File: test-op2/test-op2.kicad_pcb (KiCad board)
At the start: 2 copper layers, 167 parts, among them P1 In1, P10 Out2, P11 Out3, P12 Out4, P13 CONN_13X2, P14 CONN_5X2, P2 In2, P3 In3, P4 In4, P5 HOLD3, P6 RST3, P7 HOLD4, P8 RST4, P9 Out1, U1 LM7171, U10 LM7171, U11 LMH6505, U12 LMH6505, U13 DG467, U14 DG468, U15 LM7171, U16 LMH6505, U17 LMH6505, U2 LMH6505, U3 LMH6505, U4 LM7171, U5 LMH6505, U6 LMH6505, U7 DG467, U8 DG468, U9 LM7171

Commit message: [test-op2] layout
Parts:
- moved C64 0.13 mm to (148.2, 39.2), turned to 0 degrees
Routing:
- net GND: track 137.5 -> 957.2 mm, vias 0 -> 13
- net +5V: track 40.8 -> 382.2 mm, vias 0 -> 11
- net -5V: track 32.8 -> 258.6 mm, vias 0 -> 19
- net Off1_3: track 2.35 -> 192.0 mm, vias 0 -> 1
- net +15V: track 11.4 -> 193.0 mm, vias 0 -> 1
- net Ctrl1_1: track 0.00 -> 135.0 mm, vias 0 -> 1
- net Off1_4: track 2.17 -> 136.6 mm, vias 0 -> 1
- net -15V: track 13.4 -> 132.7 mm, vias 0 -> 7
- net Off2_1: track 3.53 -> 108.6 mm
- net Ctrl1_4: track 0.00 -> 97.7 mm, vias 0 -> 4
- net Off1_1: track 2.43 -> 98.7 mm
- net Off2_4: track 1.99 -> 96.6 mm, vias 0 -> 1
- net Off1_2: track 2.43 -> 93.4 mm, vias 0 -> 1
- net Off3_4: track 0.00 -> 89.8 mm, vias 0 -> 2
- net Off4_1: track 2.63 -> 86.9 mm, vias 0 -> 1
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- added copper zone on B.Cu, net GND
- added copper zone on F.Cu, net GND

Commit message: [test-op2] tweak
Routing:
- net Off1_3: track 192.0 -> 192.8 mm
- net Off1_4: track 136.6 -> 137.3 mm
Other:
- board outline added: 137.8 x 75.6 mm

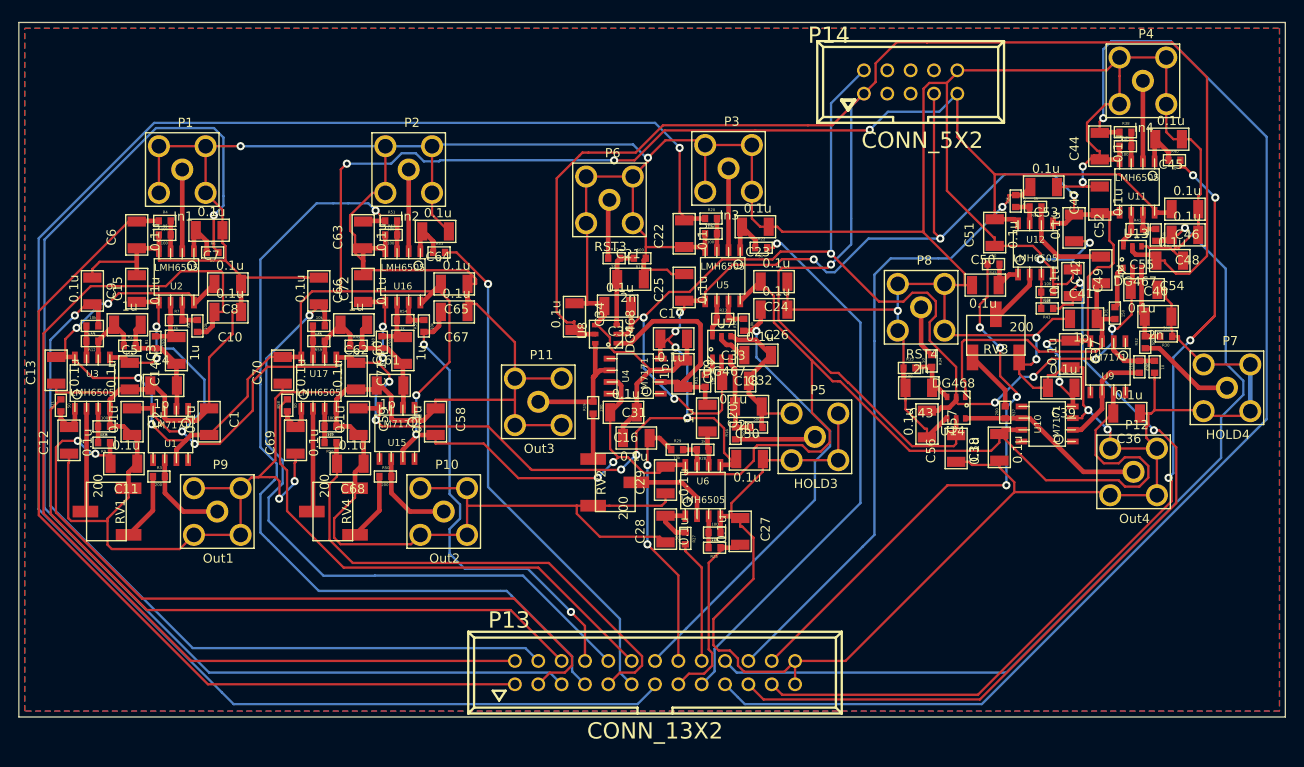
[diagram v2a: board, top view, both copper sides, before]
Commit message: [test-op2] more compact layout
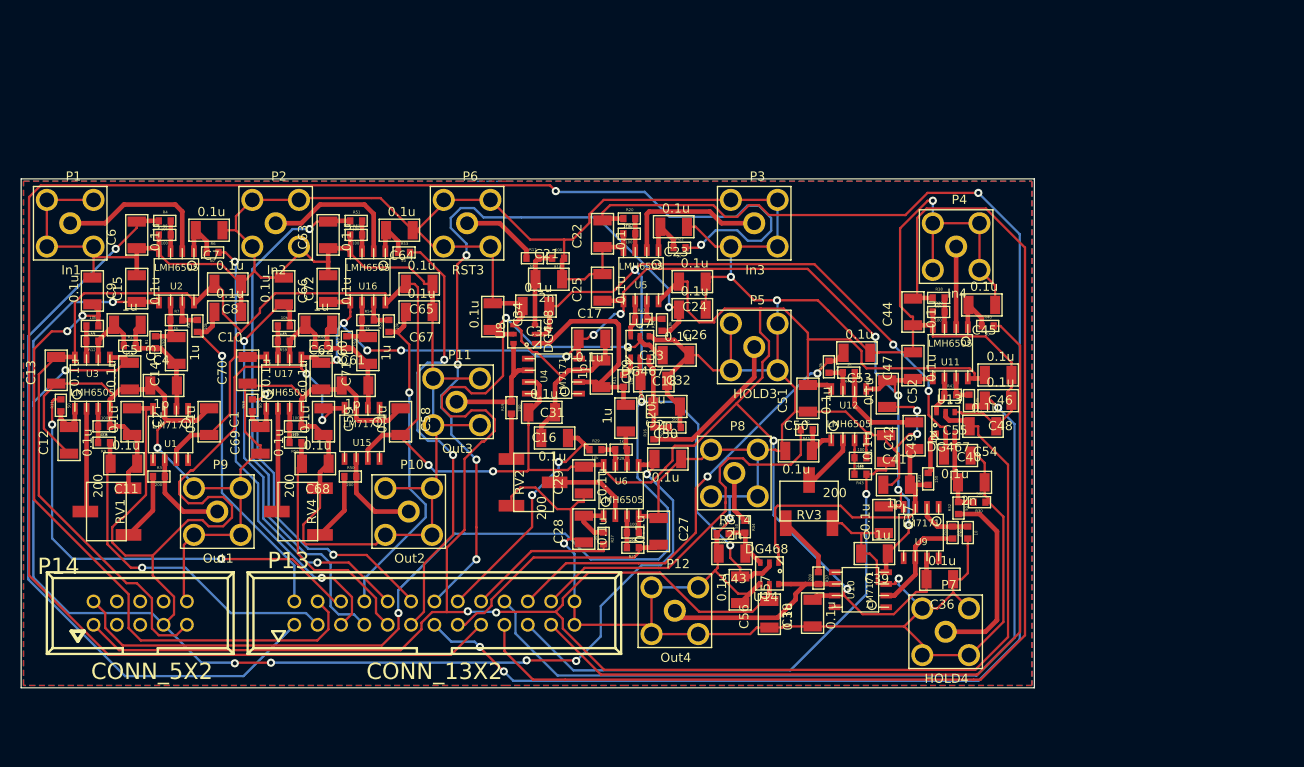
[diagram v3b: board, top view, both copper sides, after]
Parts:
- moved P14 101.8 mm to (116.1, 80.8)
- moved P12 52.1 mm to (174.2, 80.5)
- moved P7 40.5 mm to (203.7, 82.8)
- moved C38 27.2 mm to (189.2, 80.8)
- moved C44 27.2 mm to (200.2, 48.0)
- moved C47 27.2 mm to (200.2, 53.8)
- moved C50 27.2 mm to (187.7, 63.1)
- moved C54 27.2 mm to (207.8, 60.5)
- moved R32 27.2 mm to (205.1, 69.3)
- moved R42 27.2 mm to (206.2, 57.7)
- moved RV3 27.2 mm to (188.8, 68.6)
- moved R30 27.2 mm to (207.4, 68.7)
- moved C41 27.2 mm to (198.4, 66.8)
- moved C42 27.2 mm to (200.3, 61.5)
- moved C51 27.2 mm to (188.7, 57.4)
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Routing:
- net GND: track 957.2 -> 793.1 mm, vias 13 -> 9
- net Ctrl1_3: track 60.5 -> 191.5 mm, vias 1 -> 2
- net -5V: track 258.6 -> 365.0 mm, vias 19 -> 20
- net Ctrl1_1: track 135.0 -> 48.6 mm, vias 1 -> 2
- net +5V: track 382.2 -> 305.2 mm, vias 11 -> 4
- net Off2_1: track 108.6 -> 37.3 mm, vias 0 -> 1
- net -15V: track 132.7 -> 203.8 mm, vias 7 -> 6
- net Off3_1: track 84.4 -> 37.7 mm, vias 2 -> 1
- net +15V: track 193.0 -> 234.4 mm, vias 1 -> 4
- net Off1_2: track 93.4 -> 58.5 mm
- net Off3_4: track 89.8 -> 58.6 mm, vias 2 -> 1
- net Off2_3: track 51.1 -> 81.7 mm, vias 1 -> 5
- net Off3_2: track 55.7 -> 26.2 mm
- net Off1_3: track 192.8 -> 165.5 mm, vias 1 -> 3
- net Off4_2: track 73.2 -> 46.1 mm, vias 1 -> 2
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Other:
- board size 137.8 x 75.6 mm -> 110.2 x 55.4 mm
